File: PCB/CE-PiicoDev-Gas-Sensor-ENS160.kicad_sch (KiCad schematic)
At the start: 24 parts, among them J1 , J2 , J3 Conn_01x05_Male, U1 ENS160, U2 Regulator 1V8

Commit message: v00
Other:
- title: (none) -> PiicoDev Air Quality Sensor
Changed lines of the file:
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@@
   (paper "A4")
   (title_block
+    (title "PiicoDev Air Quality Sensor")
+    (date "2022-05-04")
+    (rev "00")
     (company "Core Electronics")
+    (comment 1 "Designed by Peter Johnston at")
+    (comment 2 "PiicoDev and the PiicoDev logo are trademarks of Core Electronics Pty Ltd.")
+    (comment 3 "License: CCASAv4.0 http://creativecommons.org/licenses/by-sa/4.0")
   )
   (junction (at 138.43 36.83) (diameter 0) (color 0 0 0 0)

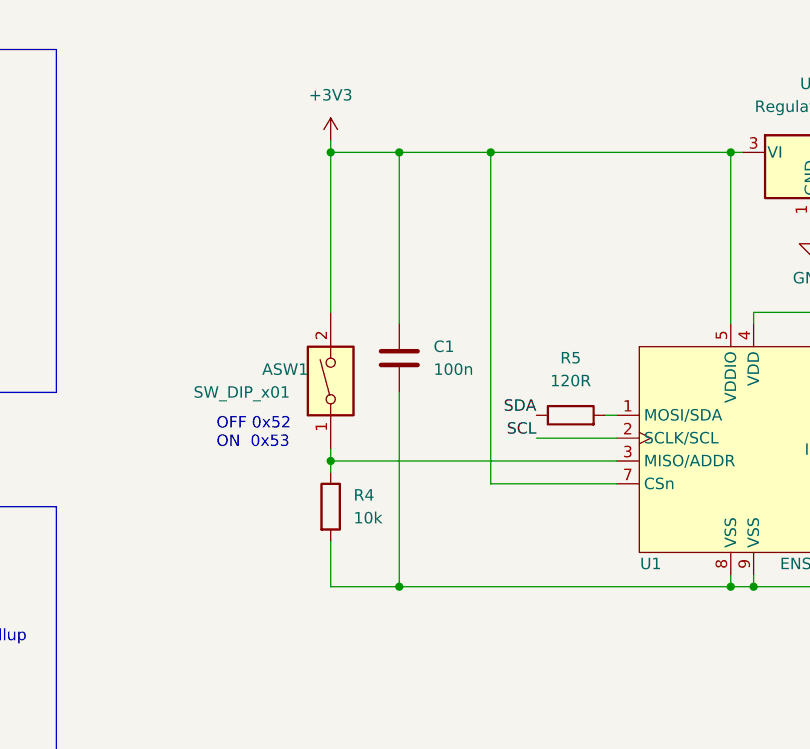
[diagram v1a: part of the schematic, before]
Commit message: Change default I2C address
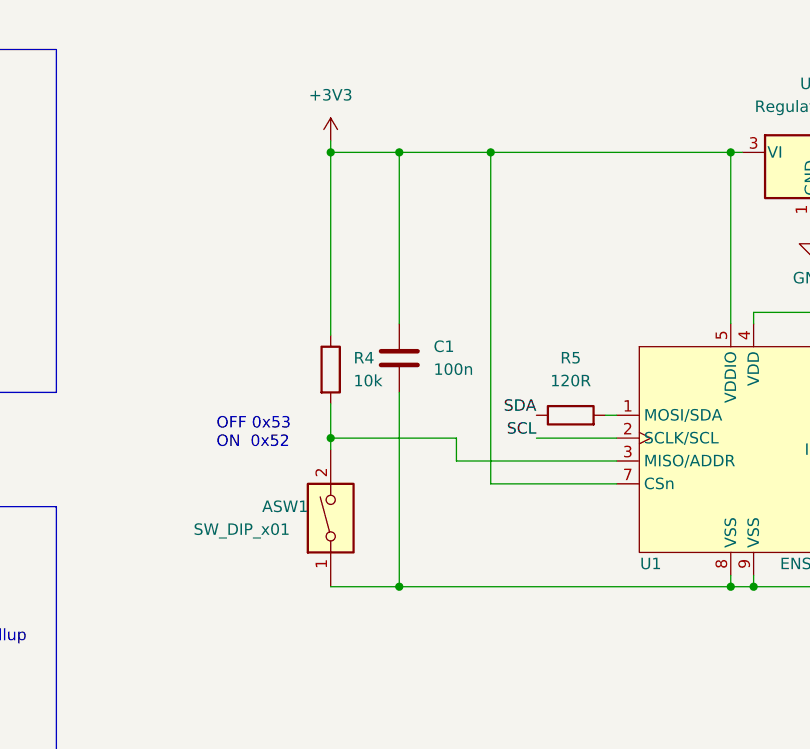
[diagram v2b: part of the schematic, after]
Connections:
- net +3V3: now also R4.1; no longer ASW1.2
- net GND: now also ASW1.1; no longer R4.2
- new net: ASW1.2, R4.2, U1.3 (MISO/ADDR)
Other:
- note added: "OFF 0x53 ON 0x52"
- note removed: "OFF 0x52 ON 0x53"
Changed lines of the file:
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@@
   (title_block
     (title "PiicoDev Air Quality Sensor")
-    (date "2022-05-04")
-    (rev "00")
+    (date "2022-06-21")
+    (rev "01")
     (company "Core Electronics")
     (comment 1 "Designed by Peter Johnston at")
@@
   (junction (at 138.43 36.83) (diameter 0) (color 0 0 0 0)
   )
+  (junction (at 130.81 36.83) (diameter 0) (color 0 0 0 0)
+  )
   (junction (at 175.26 36.83) (diameter 0) (color 0 0 0 0)
   )
   (junction (at 177.8 85.09) (diameter 0) (color 0 0 0 0)
   )
-  (junction (at 130.81 71.12) (diameter 0) (color 0 0 0 0)
+  (junction (at 130.81 68.58) (diameter 0) (color 0 0 0 0)
   )
   (junction (at 175.26 85.09) (diameter 0) (color 0 0 0 0)
@@
   (junction (at 148.59 36.83) (diameter 0) (color 0 0 0 0)
   )
-  (junction (at 130.81 36.83) (diameter 0) (color 0 0 0 0)
-  )
   (junction (at 193.04 85.09) (diameter 0) (color 0 0 0 0)
   )
@@
     (stroke (width 0) (type default) (color 0 0 0 0))
   )
-  (wire (pts (xy 130.81 71.12) (xy 130.81 72.39))
-    (stroke (width 0) (type default) (color 0 0 0 0))
-  )
   (wire (pts (xy 193.04 54.61) (xy 193.04 55.88))
     (stroke (width 0) (type default) (color 0 0 0 0))
@@
     (stroke (width 0) (type default) (color 0 0 0 0))
   )
-  (wire (pts (xy 130.81 69.85) (xy 130.81 71.12))
-    (stroke (width 0) (type default) (color 0 0 0 0))
-  )
   (wire (pts (xy 130.81 85.09) (xy 138.43 85.09))
     (stroke (width 0) (type default) (color 0 0 0 0))
@@
     (stroke (width 0) (type default) (color 0 0 0 0))
   )
-  (wire (pts (xy 130.81 36.83) (xy 130.81 54.61))
-    (stroke (width 0) (type default) (color 0 0 0 0))
-  )
   (wire (pts (xy 138.43 63.5) (xy 138.43 85.09))
     (stroke (width 0) (type default) (color 0 0 0 0))
@@
     (stroke (width 0) (type default) (color 0 0 0 0))
   )
+  (wire (pts (xy 130.81 64.77) (xy 130.81 68.58))
+    (stroke (width 0) (type default) (color 0 0 0 0))
+  )
   (wire (pts (xy 82.55 107.95) (xy 82.55 118.11))
     (stroke (width 0) (type default) (color 0 0 0 0))
@@
     (stroke (width 0) (type default) (color 0 0 0 0))
   )
-  (wire (pts (xy 130.81 80.01) (xy 130.81 85.09))
-    (stroke (width 0) (type default) (color 0 0 0 0))
-  )
   (wire (pts (xy 36.83 96.52) (xy 36.83 95.25))
     (stroke (width 0) (type default) (color 0 0 0 0))
@@
     (stroke (width 0) (type default) (color 0 0 0 0))
   )
-  (wire (pts (xy 130.81 71.12) (xy 162.56 71.12))
-    (stroke (width 0) (type default) (color 0 0 0 0))
-  )
   (polyline (pts (xy 63.5 76.2) (xy 100.33 76.2))
     (stroke (width 0) (type default) (color 0 0 0 0))
@@
     (stroke (width 0) (type default) (color 0 0 0 0))
   )
+  (wire (pts (xy 130.81 68.58) (xy 130.81 69.85))
+    (stroke (width 0) (type default) (color 0 0 0 0))
+  )
   (polyline (pts (xy 25.4 25.4) (xy 62.23 25.4))
     (stroke (width 0) (type default) (color 0 0 0 0))
@@
     (stroke (width 0) (type default) (color 0 0 0 0))
   )
+  (wire (pts (xy 144.78 68.58) (xy 144.78 71.12))
+    (stroke (width 0) (type default) (color 0 0 0 0))
+  )
   (wire (pts (xy 130.81 36.83) (xy 138.43 36.83))
     (stroke (width 0) (type default) (color 0 0 0 0))
@@
     (stroke (width 0) (type default) (color 0 0 0 0))
   )
+  (wire (pts (xy 130.81 36.83) (xy 130.81 57.15))
+    (stroke (width 0) (type default) (color 0 0 0 0))
+  )
   (polyline (pts (xy 134.62 196.85) (xy 154.94 196.85))
     (stroke (width 0) (type default) (color 0 0 0 0))
   )
+  (wire (pts (xy 144.78 71.12) (xy 162.56 71.12))
+    (stroke (width 0) (type default) (color 0 0 0 0))
+  )
   (wire (pts (xy 82.55 118.11) (xy 93.98 118.11))
     (stroke (width 0) (type default) (color 0 0 0 0))
@@
   )
   (wire (pts (xy 36.83 105.41) (xy 36.83 104.14))
+    (stroke (width 0) (type default) (color 0 0 0 0))
+  )
+  (wire (pts (xy 130.81 68.58) (xy 144.78 68.58))
     (stroke (width 0) (type default) (color 0 0 0 0))
   )
@@
     (effects (font (size 1.27 1.27)) (justify left bottom))
   )
-  (text "OFF 0x52\nON  0x53" (at 118.11 69.85 0)
+  (text "OFF 0x53\nON  0x52" (at 118.11 69.85 0)
     (effects (font (size 1.27 1.27)) (justify left bottom))
   )
@@
     )
     (pin "1")
+  )
+  (symbol (lib_id "Switch:SW_DIP_x01") (at 130.81 77.47 90) (unit 1)
+    (in_bom yes) (on_board yes)
+    (property "Reference" "ASW1" (id 0) (at 123.19 76.2 90)
+      (effects (font (size 1.27 1.27)) (justify right))
+    )
+    (property "Value" "SW_DIP_x01" (id 1) (at 115.57 78.74 90)
+      (effects (font (size 1.27 1.27)) (justify right))
+    )
+    (property "Footprint" "CoreElectronics_Components:SW_DIP_x01_Slide_CHS-01A1" (id 2) (at 130.81 77.47 0)
+      (effects (font (size 1.27 1.27)) hide)
+    )
+    (property "Datasheet" "~" (id 3) (at 130.81 77.47 0)
+      (effects (font (size 1.27 1.27)) hide)
+    )
+    (pin "1")
+    (pin "2")
   )
   (symbol (lib_id "Regulator_Linear:XC6206PxxxMR") (at 184.15 36.83 0) (unit 1)
@@
     )
     (property "Datasheet" "~" (id 3) (at 193.04 59.69 0)
-      (effects (font (size 1.27 1.27)) hide)
-    )
-    (pin "1")
-    (pin "2")
-  )
-  (symbol (lib_id "Switch:SW_DIP_x01") (at 130.81 62.23 90) (unit 1)
-    (in_bom yes) (on_board yes)
-    (property "Reference" "ASW1" (id 0) (at 123.19 60.96 90)
-      (effects (font (size 1.27 1.27)) (justify right))
-    )
-    (property "Value" "SW_DIP_x01" (id 1) (at 115.57 63.5 90)
-      (effects (font (size 1.27 1.27)) (justify right))
-    )
-    (property "Footprint" "CoreElectronics_Components:SW_DIP_x01_Slide_CHS-01A1" (id 2) (at 130.81 62.23 0)
-      (effects (font (size 1.27 1.27)) hide)
-    )
-    (property "Datasheet" "~" (id 3) (at 130.81 62.23 0)
       (effects (font (size 1.27 1.27)) hide)
     )
@@
     (pin "9")
   )
-  (symbol (lib_id "Device:R") (at 130.81 76.2 0) (unit 1)
+  (symbol (lib_id "Device:R") (at 130.81 60.96 0) (unit 1)
     (in_bom yes) (on_board yes) (fields_autoplaced)
-    (property "Reference" "R4" (id 0) (at 133.35 74.9299 0)
-      (effects (font (size 1.27 1.27)) (justify left))
-    )
-    (property "Value" "10k" (id 1) (at 133.35 77.4699 0)
-      (effects (font (size 1.27 1.27)) (justify left))
-    )
-    (property "Footprint" "Resistor_SMD:R_0402_1005Metric" (id 2) (at 129.032 76.2 90)
-      (effects (font (size 1.27 1.27)) hide)
-    )
-    (property "Datasheet" "~" (id 3) (at 130.81 76.2 0)
+    (property "Reference" "R4" (id 0) (at 133.35 59.6899 0)
+      (effects (font (size 1.27 1.27)) (justify left))
+    )
+    (property "Value" "10k" (id 1) (at 133.35 62.2299 0)
+      (effects (font (size 1.27 1.27)) (justify left))
+    )
+    (property "Footprint" "Resistor_SMD:R_0402_1005Metric" (id 2) (at 129.032 60.96 90)
+      (effects (font (size 1.27 1.27)) hide)
+    )
+    (property "Datasheet" "~" (id 3) (at 130.81 60.96 0)
       (effects (font (size 1.27 1.27)) hide)
     )
@@
       (reference "#PWR0111") (unit 1) (value "+3V3") (footprint "")
     )
-    (path "/69b94860-24f5-4340-801c-3f418099360d"
+    (path "/56641dfd-5e5e-4d8e-941e-5ce7952d61a3"
       (reference "ASW1") (unit 1) (value "SW_DIP_x01") (footprint "CoreElectronics_Components:SW_DIP_x01_Slide_CHS-01A1")
     )
@@
       (reference "R3") (unit 1) (value "10k") (footprint "Resistor_SMD:R_0402_1005Metric")
     )
-    (path "/bd193a59-8018-4194-9c64-8a0de648eec5"
+    (path "/a9deff47-2ea0-41df-bd56-8d8b11c744b6"
       (reference "R4") (unit 1) (value "10k") (footprint "Resistor_SMD:R_0402_1005Metric")
     )
